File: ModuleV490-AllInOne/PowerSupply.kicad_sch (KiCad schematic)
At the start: 28 parts, among them J5 POWER_IN, J9 BYPASS, U10 XL7005A, U11 AP2204K-5.0TRG1, U12 XC6206-1.8NR, U9 XC6206-3.3V

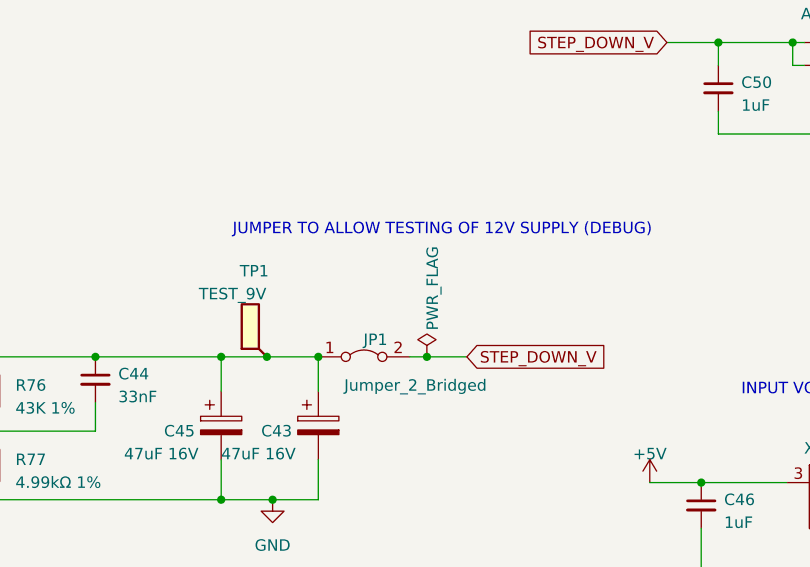
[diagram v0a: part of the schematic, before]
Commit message: Change JP1 jumper to single pin (remove part) and SPI debug pins
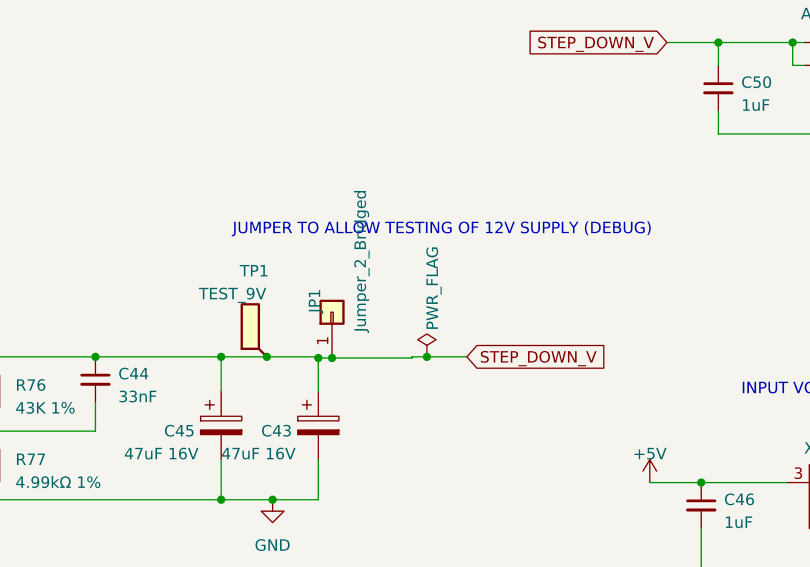
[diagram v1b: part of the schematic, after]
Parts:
- JP1: footprint Connector_PinHeader_2.54mm:PinHeader_1x02_P2.54mm_Vertical -> Connector_PinHeader_2.54mm:PinHeader_1x01_P2.54mm_Vertical; symbol Jumper:Jumper_2_Bridged -> Connector_Generic:Conn_01x01
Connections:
- net STEP_DOWN_V: now also C43.1, C44.1, C45.1, JP1.1 (Pin_1), L1.2, R76.1, TP1.1; no longer JP1.2 (B)
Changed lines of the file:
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@@
   (junction (at 229.87 38.1) (diameter 0) (color 0 0 0 0)
   )
+  (junction (at 150.114 73.152) (diameter 0) (color 0 0 0 0)
+  )
   (junction (at 208.28 97.155) (diameter 0) (color 0 0 0 0)
   )
   (junction (at 228.6 121.285) (diameter 0) (color 0 0 0 0)
   )
-  (junction (at 148.59 73.025) (diameter 0) (color 0 0 0 0)
-  )
   (junction (at 210.185 48.26) (diameter 0) (color 0 0 0 0)
   )
@@
   (junction (at 221.615 38.1) (diameter 0) (color 0 0 0 0)
   )
+  (junction (at 148.59 73.152) (diameter 0) (color 0 0 0 0)
+  )
   (junction (at 83.82 84.455) (diameter 0) (color 0 0 0 0)
   )
@@
     (stroke (width 0) (type default))
   )
+  (wire (pts (xy 148.59 73.025) (xy 148.59 73.152))
+    (stroke (width 0) (type default))
+  )
   (wire (pts (xy 88.9 84.455) (xy 95.885 84.455))
     (stroke (width 0) (type default))
@@
     (stroke (width 0) (type default))
   )
+  (wire (pts (xy 159.004 73.025) (xy 160.655 73.025))
+    (stroke (width 0) (type default))
+  )
   (wire (pts (xy 92.075 81.28) (xy 92.075 82.55))
     (stroke (width 0) (type default))
@@
     (stroke (width 0) (type default))
   )
-  (wire (pts (xy 158.75 73.025) (xy 160.655 73.025))
+  (wire (pts (xy 150.114 73.152) (xy 159.004 73.152))
     (stroke (width 0) (type default))
   )
@@
     (stroke (width 0) (type default))
   )
-  (wire (pts (xy 148.59 73.025) (xy 148.59 76.835))
-    (stroke (width 0) (type default))
-  )
   (wire (pts (xy 72.39 75.565) (xy 70.485 75.565))
     (stroke (width 0) (type default))
@@
     (stroke (width 0) (type default))
   )
+  (wire (pts (xy 159.004 73.152) (xy 159.004 73.025))
+    (stroke (width 0) (type default))
+  )
   (wire (pts (xy 112.395 73.025) (xy 112.395 74.295))
     (stroke (width 0) (type default))
@@
     (stroke (width 0) (type default))
   )
+  (wire (pts (xy 150.114 73.152) (xy 148.59 73.152))
+    (stroke (width 0) (type default))
+  )
   (wire (pts (xy 64.135 81.915) (xy 64.135 84.455))
     (stroke (width 0) (type default))
@@
   )
   (wire (pts (xy 86.36 84.455) (xy 88.9 84.455))
+    (stroke (width 0) (type default))
+  )
+  (wire (pts (xy 148.59 73.152) (xy 148.59 76.835))
     (stroke (width 0) (type default))
   )
@@
     )
   )
-  (symbol (lib_id "Jumper:Jumper_2_Bridged") (at 153.67 73.025 0) (unit 1)
+  (symbol (lib_id "Connector_Generic:Conn_01x01") (at 150.114 68.072 90) (unit 1)
     (in_bom yes) (on_board yes) (dnp no)
-    (property "Reference" "JP1" (at 154.94 71.12 0)
-      (effects (font (size 1.27 1.27)))
-    )
-    (property "Value" "Jumper_2_Bridged" (at 159.385 76.2 0)
-      (effects (font (size 1.27 1.27)))
-    )
-    (property "Footprint" "Connector_PinHeader_2.54mm:PinHeader_1x02_P2.54mm_Vertical" (at 153.67 73.025 0)
-      (effects (font (size 1.27 1.27)) hide)
-    )
-    (property "Datasheet" "~" (at 153.67 73.025 0)
-      (effects (font (size 1.27 1.27)) hide)
-    )
-    (property "PartNumber" "DZ254R-11-02-63" (at 153.67 73.025 0)
-      (effects (font (size 1.27 1.27)) hide)
-    )
-    (property "LCSCStockCode" "C2935908" (at 153.67 73.025 0)
-      (effects (font (size 1.27 1.27)) hide)
-    )
-    (pin "1")
-    (pin "2")
-    (instances
-      (project "Module_16S"
+    (property "Reference" "JP1" (at 148.209 66.802 0)
+      (effects (font (size 1.27 1.27)))
+    )
+    (property "Value" "Jumper_2_Bridged" (at 153.289 62.357 0)
+      (effects (font (size 1.27 1.27)))
+    )
+    (property "Footprint" "Connector_PinHeader_2.54mm:PinHeader_1x01_P2.54mm_Vertical" (at 150.114 68.072 0)
+      (effects (font (size 1.27 1.27)) hide)
+    )
+    (property "Datasheet" "~" (at 150.114 68.072 0)
+      (effects (font (size 1.27 1.27)) hide)
+    )
+    (property "PartNumber" "DZ254R-11-02-63" (at 150.114 68.072 0)
+      (effects (font (size 1.27 1.27)) hide)
+    )
+    (property "LCSCStockCode" "C2935908" (at 150.114 68.072 0)
+      (effects (font (size 1.27 1.27)) hide)
+    )
+    (pin "1")
+    (instances
+      (project "Module_16S"
